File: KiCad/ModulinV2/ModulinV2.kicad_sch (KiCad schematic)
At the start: 0 parts

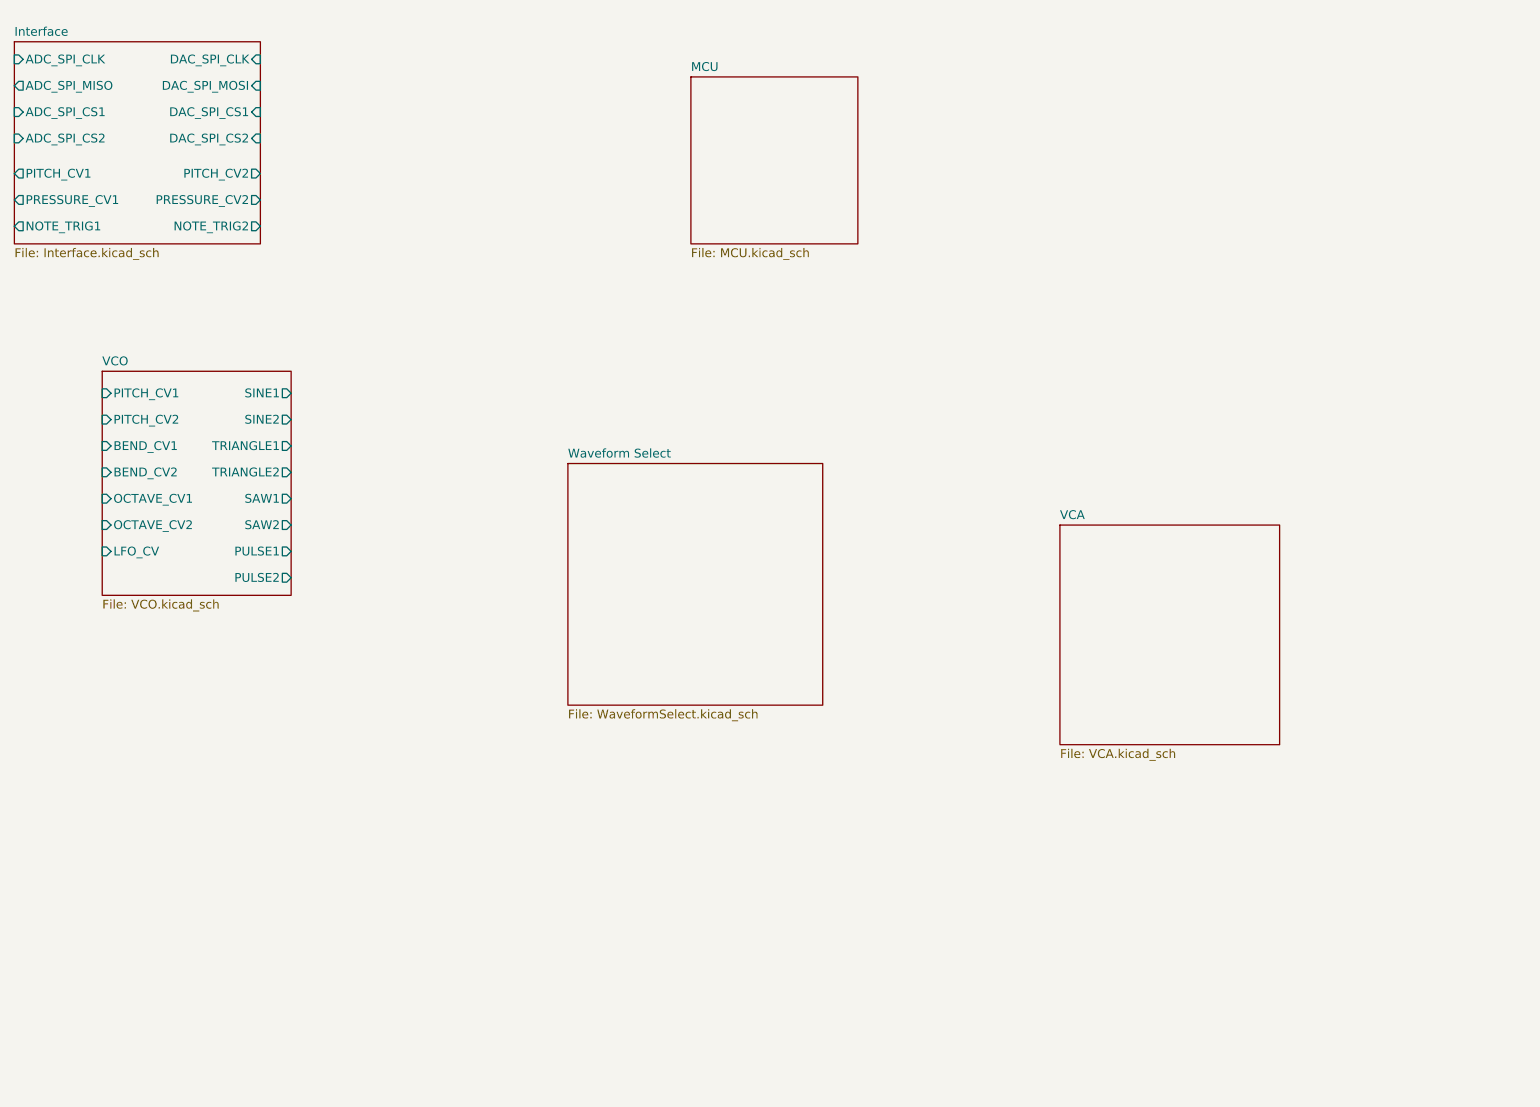
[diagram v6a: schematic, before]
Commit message: Modified Octave selector and started on waveform selection
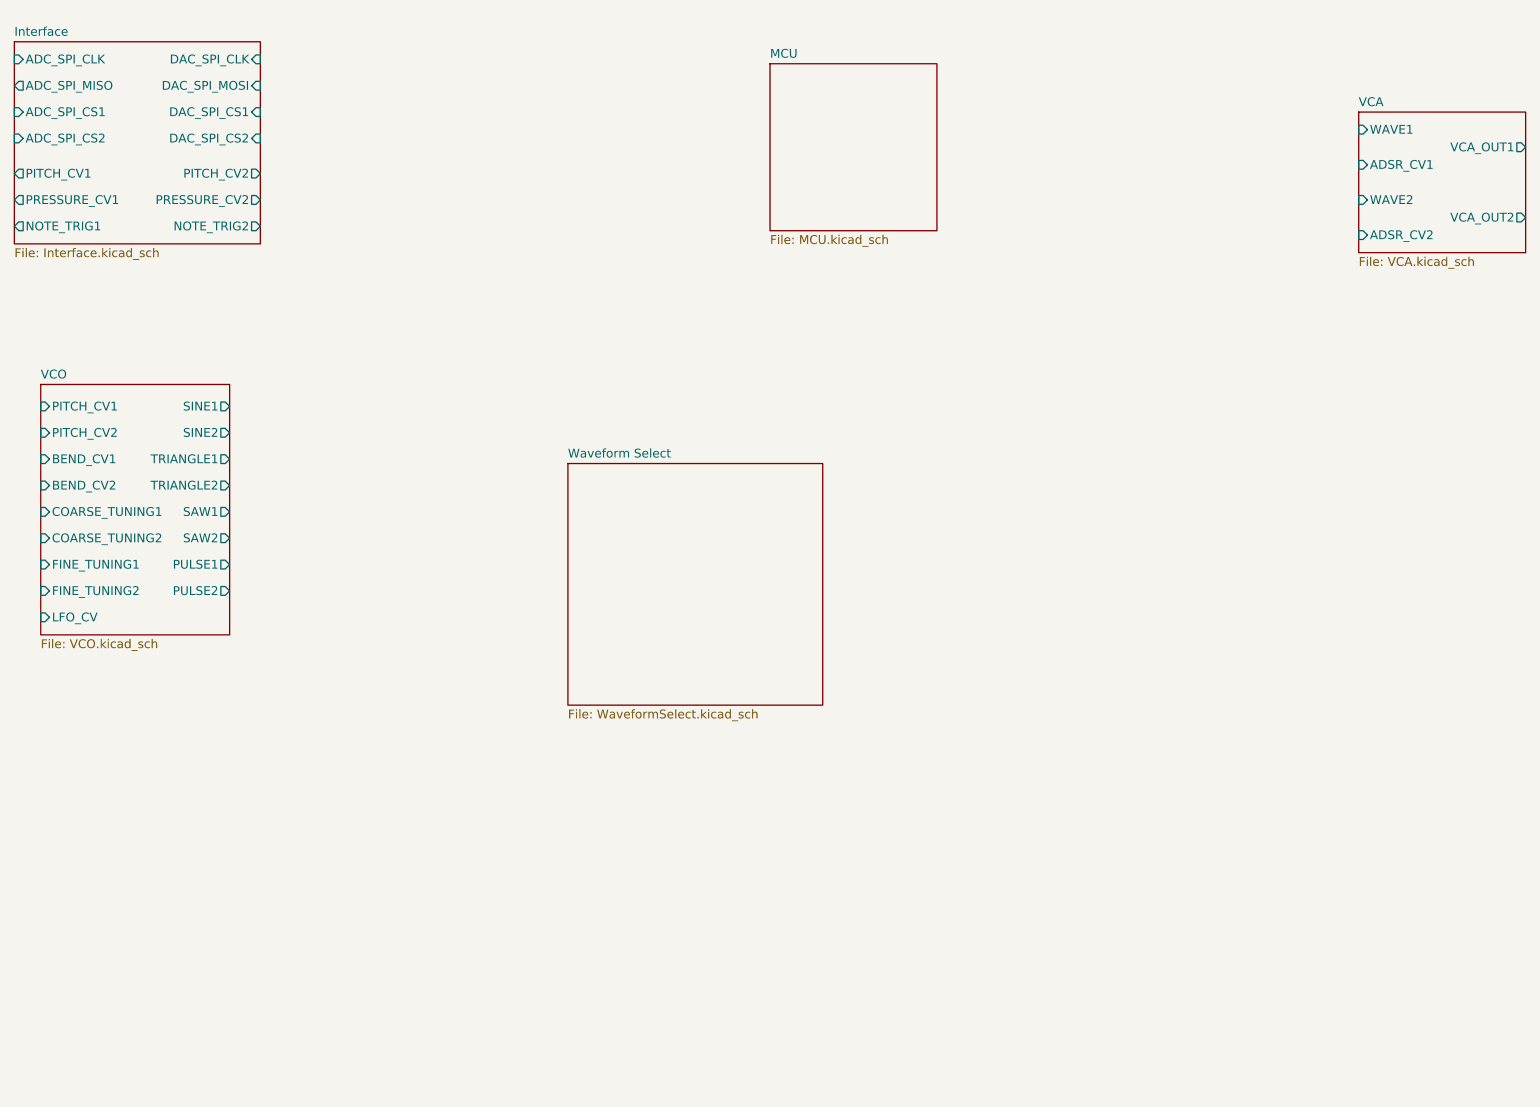
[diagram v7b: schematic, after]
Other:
- sheet VCA ports: added ADSR_CV1, ADSR_CV2, VCA_OUT1, VCA_OUT2, WAVE1, WAVE2; removed none
- sheet VCO ports: added COARSE_TUNING1, COARSE_TUNING2, FINE_TUNING1, FINE_TUNING2; removed OCTAVE_CV1, OCTAVE_CV2
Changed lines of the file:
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@@
 	)
 	(sheet
-		(at 119.38 34.29)
+		(at 130.81 32.385)
 		(size 24.13 24.13)
 		(exclude_from_sim no)
@@
 		)
 		(property "Sheetname" "MCU"
-			(at 119.38 33.5784 0)
+			(at 130.81 31.6734 0)
 			(show_name yes)
 			(effects
@@
 		)
 		(property "Sheetfile" "MCU.kicad_sch"
-			(at 119.38 59.0046 0)
+			(at 130.81 57.0996 0)
 			(effects
 				(font
@@
 	)
 	(sheet
-		(at 34.29 76.835)
-		(size 27.305 32.385)
+		(at 25.4 78.74)
+		(size 27.305 36.195)
 		(exclude_from_sim no)
 		(in_bom yes)
@@
 		)
 		(property "Sheetname" "VCO"
-			(at 34.29 76.1234 0)
+			(at 25.4 78.0284 0)
 			(effects
 				(font
@@
 		)
 		(property "Sheetfile" "VCO.kicad_sch"
-			(at 34.29 109.8046 0)
+			(at 25.4 115.5196 0)
 			(effects
 				(font
@@
 		)
 		(pin "LFO_CV" input
-			(at 34.29 102.87 180)
+			(at 25.4 112.395 180)
 			(effects
 				(font
@@
 		)
 		(pin "PULSE1" output
-			(at 61.595 102.87 0)
+			(at 52.705 104.775 0)
 			(effects
 				(font
@@
 		)
 		(pin "PULSE2" output
-			(at 61.595 106.68 0)
+			(at 52.705 108.585 0)
 			(effects
 				(font
@@
 		)
 		(pin "TRIANGLE2" output
-			(at 61.595 91.44 0)
+			(at 52.705 93.345 0)
 			(effects
 				(font
@@
 		)
 		(pin "SAW2" output
-			(at 61.595 99.06 0)
+			(at 52.705 100.965 0)
 			(effects
 				(font
@@
 		)
 		(pin "SINE2" output
-			(at 61.595 83.82 0)
+			(at 52.705 85.725 0)
 			(effects
 				(font
@@
 		)
 		(pin "SAW1" output
-			(at 61.595 95.25 0)
+			(at 52.705 97.155 0)
 			(effects
 				(font
@@
 		)
 		(pin "SINE1" output
-			(at 61.595 80.01 0)
+			(at 52.705 81.915 0)
 			(effects
 				(font
@@
 		)
 		(pin "TRIANGLE1" output
-			(at 61.595 87.63 0)
+			(at 52.705 89.535 0)
 			(effects
 				(font
@@
 		)
 		(pin "PITCH_CV1" input
-			(at 34.29 80.01 180)
+			(at 25.4 81.915 180)
 			(effects
 				(font
@@
 		)
 		(pin "PITCH_CV2" input
-			(at 34.29 83.82 180)
+			(at 25.4 85.725 180)
 			(effects
 				(font
@@
 		)
 		(pin "BEND_CV2" input
-			(at 34.29 91.44 180)
-			(effects
-				(font
-					(size 1.27 1.27)
-				)
-				(justify left)
-			)
-		)
-		(pin "OCTAVE_CV2" input
-			(at 34.29 99.06 180)
-			(effects
-				(font
-					(size 1.27 1.27)
-				)
-				(justify left)
-			)
-		)
-		(pin "OCTAVE_CV1" input
-			(at 34.29 95.25 180)
+			(at 25.4 93.345 180)
 			(effects
 				(font
@@
 		)
 		(pin "BEND_CV1" input
-			(at 34.29 87.63 180)
+			(at 25.4 89.535 180)
+			(effects
+				(font
+					(size 1.27 1.27)
+				)
+				(justify left)
+			)
+		)
+		(pin "FINE_TUNING1" input
+			(at 25.4 104.775 180)
+			(effects
+				(font
+					(size 1.27 1.27)
+				)
+				(justify left)
+			)
+		)
+		(pin "COARSE_TUNING1" input
+			(at 25.4 97.155 180)
+			(effects
+				(font
+					(size 1.27 1.27)
+				)
+				(justify left)
+			)
+		)
+		(pin "FINE_TUNING2" input
+			(at 25.4 108.585 180)
+			(effects
+				(font
+					(size 1.27 1.27)
+				)
+				(justify left)
+			)
+		)
+		(pin "COARSE_TUNING2" input
+			(at 25.4 100.965 180)
 			(effects
 				(font
@@
 	)
 	(sheet
-		(at 172.72 99.06)
-		(size 31.75 31.75)
+		(at 215.9 39.37)
+		(size 24.13 20.32)
 		(exclude_from_sim no)
 		(in_bom yes)
@@
 		)
 		(property "Sheetname" "VCA"
-			(at 172.72 98.3484 0)
+			(at 215.9 38.6584 0)
 			(effects
 				(font
@@
 		)
 		(property "Sheetfile" "VCA.kicad_sch"
-			(at 172.72 131.3946 0)
+			(at 215.9 60.2746 0)
 			(effects
 				(font
@@
 			)
 		)
+		(pin "WAVE1" input
+			(at 215.9 41.91 180)
+			(effects
+				(font
+					(size 1.27 1.27)
+				)
+				(justify left)
+			)
+		)
+		(pin "ADSR_CV2" input
+			(at 215.9 57.15 180)
+			(effects
+				(font
+					(size 1.27 1.27)
+				)
+				(justify left)
+			)
+		)
+		(pin "ADSR_CV1" input
+			(at 215.9 46.99 180)
+			(effects
+				(font
+					(size 1.27 1.27)
+				)
+				(justify left)
+			)
+		)
+		(pin "VCA_OUT2" output
+			(at 240.03 54.61 0)
+			(effects
+				(font
+					(size 1.27 1.27)
+				)
+				(justify right)
+			)
+		)
+		(pin "VCA_OUT1" output
+			(at 240.03 44.45 0)
+			(effects
+				(font
+					(size 1.27 1.27)
+				)
+				(justify right)
+			)
+		)
+		(pin "WAVE2" input
+			(at 215.9 52.07 180)
+			(effects
+				(font
+					(size 1.27 1.27)
+				)
+				(justify left)
+			)
+		)

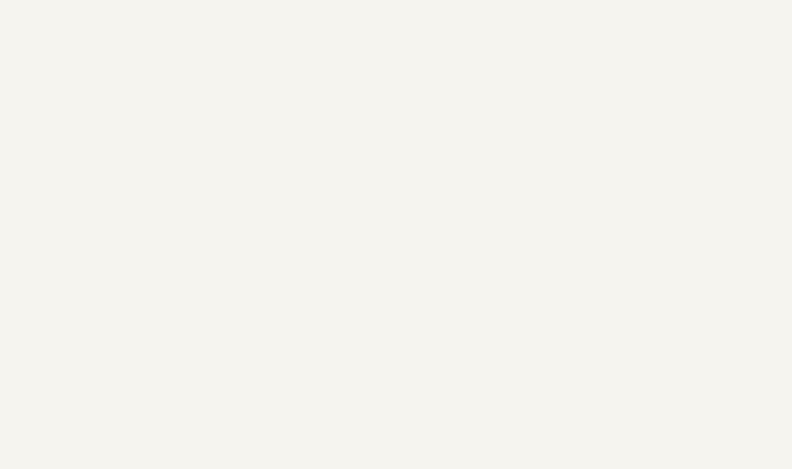
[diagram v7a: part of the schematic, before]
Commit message: Modified USB connection and added LEDs
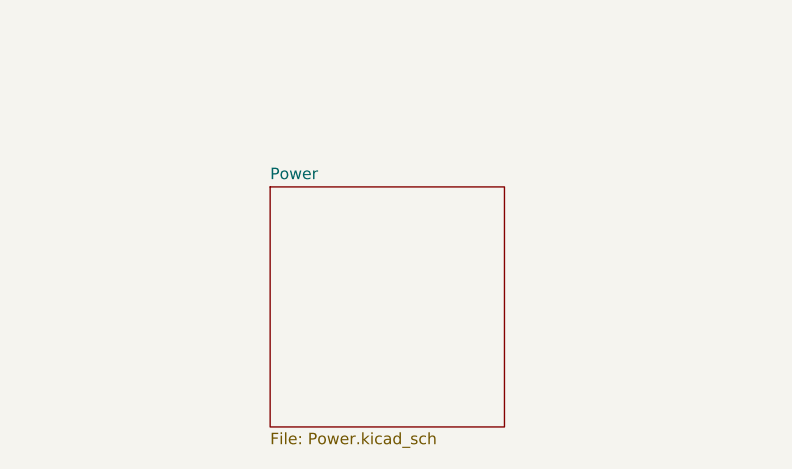
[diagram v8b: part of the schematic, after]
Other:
- added sheet Power (Power.kicad_sch)
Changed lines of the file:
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@@
+	)
+	(sheet
+		(at 49.53 151.765)
+		(size 26.035 26.67)
+		(exclude_from_sim no)
+		(in_bom yes)
+		(on_board yes)
+		(dnp no)
+		(fields_autoplaced yes)
+		(stroke
+			(width 0.1524)
+			(type solid)
+		)
+		(fill
+			(color 0 0 0 0.0000)
+		)
+		(property "Sheetname" "Power"
+			(at 49.53 151.0534 0)
+			(effects
+				(font
+					(size 1.27 1.27)
+				)
+				(justify left bottom)
+			)
+		)
+		(property "Sheetfile" "Power.kicad_sch"
+			(at 49.53 179.0196 0)
+			(effects
+				(font
+					(size 1.27 1.27)
+				)
+				(justify left top)
+			)
+		)
+		(instances
+			(project "ModulinV2"
+				(path "/c6b34a57-3941-4b56-8b80-1848c7f41082"
+					(page "8")
+				)
+			)
+		)
 	)
 	(sheet
